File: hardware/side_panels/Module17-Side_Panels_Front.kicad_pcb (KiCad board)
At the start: 2 copper layers, 103 x 30.5 mm, 1 part

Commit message: Updated HMI
Added JLCPCB placeholder for batch number, removed useless texts
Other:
- board text added: "JLCJLCJLCJLC"
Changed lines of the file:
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@@
     )
+  )
+  (gr_text "JLCJLCJLCJLC" (at 114.375 83.98) (layer "B.SilkS")
+    (effects (font (size 1 1) (thickness 0.15)) (justify mirror))
   )
   (gr_text "Reset" (at 74.745 72.975) (layer "F.SilkS")

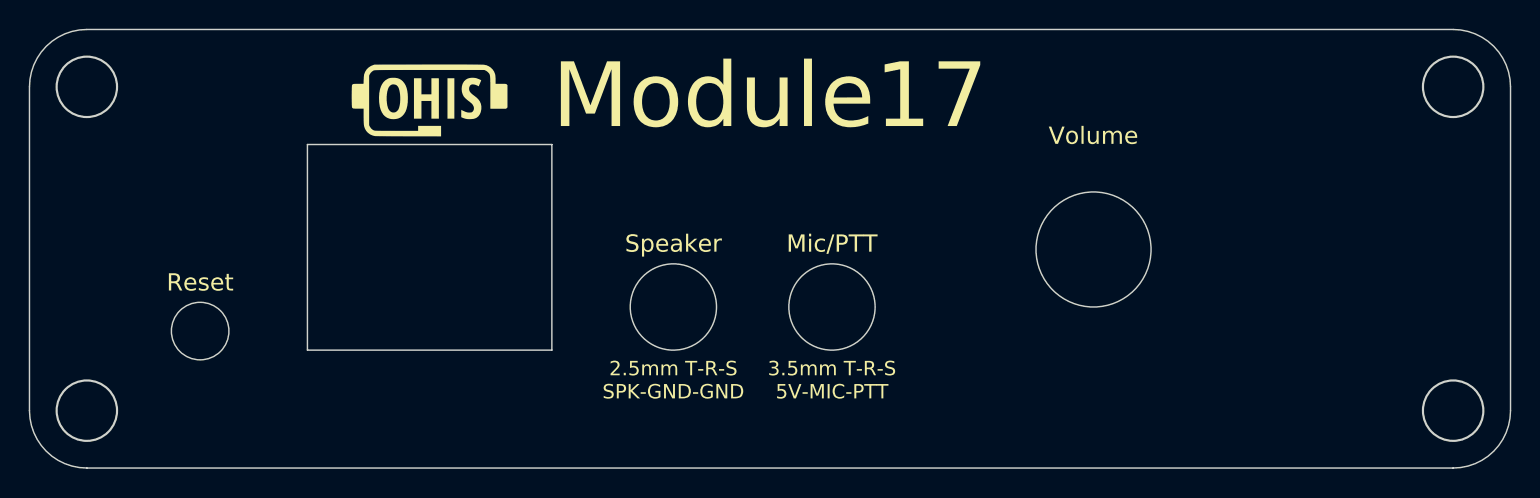
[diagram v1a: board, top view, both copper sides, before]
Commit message: Updated HMI side panels
Increased text size, added holes for the corners, added schematic title bloc plus misc. changes
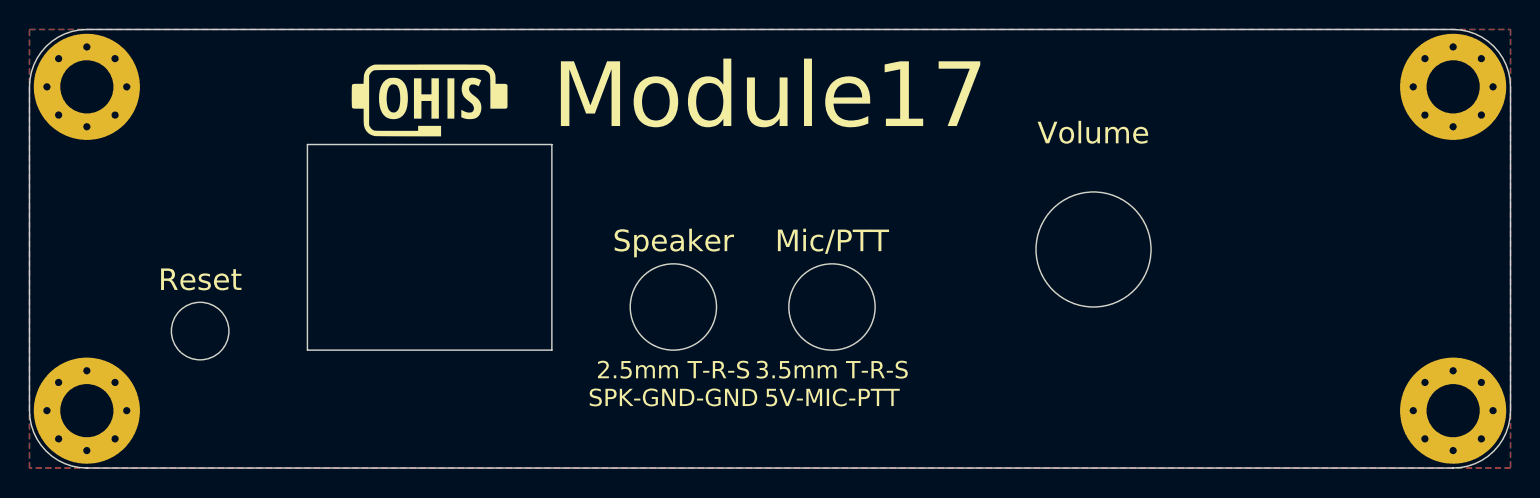
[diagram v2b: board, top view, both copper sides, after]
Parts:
- added H1: MountingHole_Pad, MountingHole:MountingHole_3.7mm_Pad_Via, F.Cu at (66.9, 58.7)
- added H2: MountingHole_Pad, MountingHole:MountingHole_3.7mm_Pad_Via, F.Cu at (66.9, 81.2)
- added H3: MountingHole_Pad, MountingHole:MountingHole_3.7mm_Pad_Via, F.Cu at (161.9, 58.7)
- added H4: MountingHole_Pad, MountingHole:MountingHole_3.7mm_Pad_Via, F.Cu at (161.9, 81.2)
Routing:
- added copper zone on B.Cu, net GND
- added copper zone on F.Cu, net GND
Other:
- outline, holes or cut-outs redrawn

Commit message: Updated Side Panels to Rev 0.99b
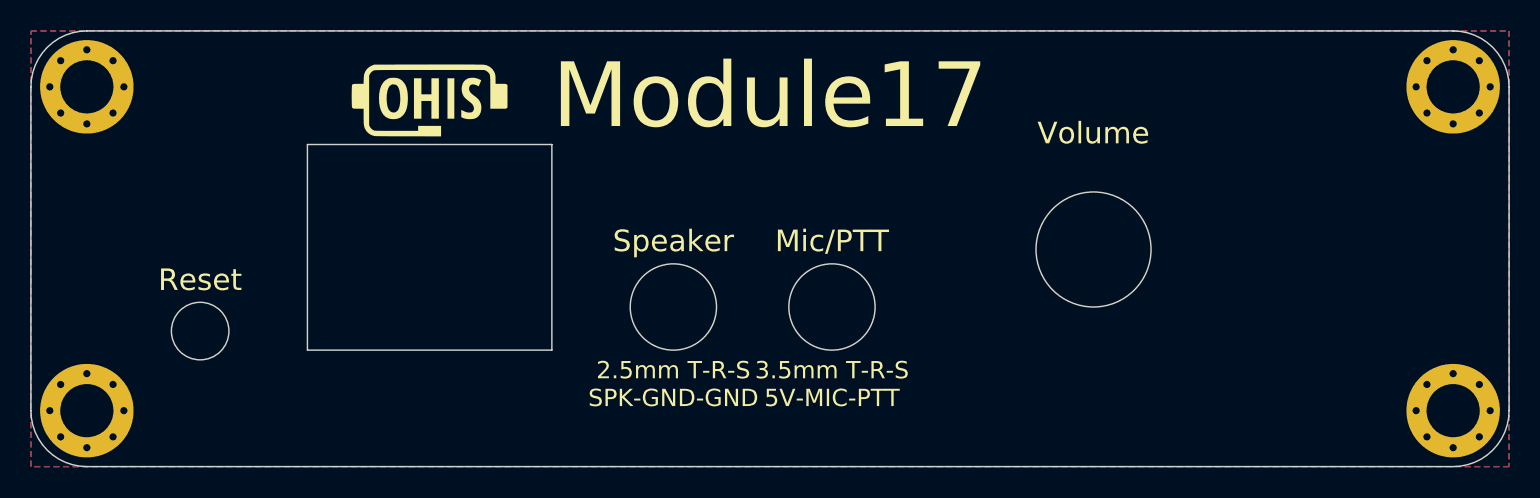
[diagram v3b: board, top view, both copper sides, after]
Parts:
- H1, H2, H3, H4: footprint MountingHole:MountingHole_3.7mm_Pad_Via -> M17_mounting_hole:MountingHole_3.7mm_Pad_Via_Small_Pad
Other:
- board size 103 x 30.5 mm -> 102.8 x 30.3 mm
- board text added: "Module17 HMI Front panel Rev 0.99b by Morgan ON4MOD"
- board text removed: "Module17 HMI Front panel Rev 0.99 by Morgan ON4MOD"

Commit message: Updated side panels PCBs to revision 1.0
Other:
- board text added: "Module17 HMI Front panel Rev 1.0 by Morgan ON4MOD"
- board text removed: "Module17 HMI Front panel Rev 0.99b by Morgan ON4MOD"
